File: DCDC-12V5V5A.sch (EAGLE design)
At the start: 30 parts, among them CN2 2828XX-2282834-2, CN3 2828XX-2282834-2, Q10 NMOSFET, Q9 NMOSFET, U1 LM3150MHX/NOPB

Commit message: Added board design. Added descriptive texts. Generated CAM files.
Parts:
- added LOGO1: RSNURL_QR_8MM, _my_logos:RSNURL_QR_8MM
- added LOGO2: MFDECLOGO_L_10MM, _my_logos:MFDECLOGO_L_10MM
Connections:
- net 5V: now also CN3.2; no longer CN3.1
- net GND: now also CN3.1; no longer CN3.2
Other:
- moved on the sheet: CN3
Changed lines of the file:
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@@
 <part name="GND3" library="SparkFun-PowerSymbols" library_urn="urn:adsk.eagle:library:530" deviceset="GND" device=""/>
 <part name="SUPPLY6" library="SparkFun-PowerSymbols" library_urn="urn:adsk.eagle:library:530" deviceset="5V" device=""/>
+<part name="LOGO1" library="_my_logos" deviceset="RSNURL" device="_QR_8MM" value="RSNURL_QR_8MM"/>
+<part name="LOGO2" library="_my_logos" deviceset="MFDECLOGO" device="_L_10MM" value="MFDECLOGO_L_10MM"/>
 </parts>
 <sheets>
@@
 <attribute name="VALUE" x="22.86" y="102.68" size="1.778" layer="95" rot="R180" align="center"/>
 </instance>
-<instance part="CN3" gate="G$1" x="241.3" y="106.68" smashed="yes">
-<attribute name="NAME" x="241.3" y="102.68" size="1.778" layer="95" align="center"/>
-<attribute name="VALUE" x="241.3" y="113.22" size="1.778" layer="95" align="center"/>
+<instance part="CN3" gate="G$1" x="241.3" y="109.22" smashed="yes" rot="MR180">
+<attribute name="NAME" x="241.3" y="113.22" size="1.778" layer="95" rot="MR180" align="center"/>
+<attribute name="VALUE" x="241.3" y="102.68" size="1.778" layer="95" rot="MR180" align="center"/>
 </instance>
 <instance part="GND1" gate="1" x="30.48" y="104.14" smashed="yes">
@@
 <attribute name="VALUE" x="233.68" y="112.014" size="1.778" layer="96" align="bottom-center"/>
 </instance>
+<instance part="LOGO1" gate="G$1" x="139.7" y="2.54" smashed="yes"/>
+<instance part="LOGO2" gate="G$1" x="109.22" y="2.54" smashed="yes"/>
 </instances>
 <busses>
@@
 </segment>
 <segment>
-<pinref part="CN3" gate="G$1" pin="2"/>
-<pinref part="GND3" gate="1" pin="GND"/>
-<wire x1="236.15" y1="106.68" x2="233.68" y2="106.68" width="0.1524" layer="91"/>
-</segment>
-<segment>
 <pinref part="GND1" gate="1" pin="GND"/>
 <pinref part="CN2" gate="G$1" pin="1"/>
@@
 <wire x1="30.48" y1="132.08" x2="30.48" y2="129.54" width="0.1524" layer="91"/>
 <junction x="30.48" y="129.54"/>
+</segment>
+<segment>
+<pinref part="CN3" gate="G$1" pin="1"/>
+<pinref part="GND3" gate="1" pin="GND"/>
+<wire x1="236.15" y1="106.68" x2="233.68" y2="106.68" width="0.1524" layer="91"/>
 </segment>
 </net>
@@
 </segment>
 <segment>
-<pinref part="CN3" gate="G$1" pin="1"/>
 <pinref part="SUPPLY6" gate="G$1" pin="5V"/>
-<wire x1="236.15" y1="109.22" x2="233.68" y2="109.22" width="0.1524" layer="91"/>
+<pinref part="CN3" gate="G$1" pin="2"/>
+<wire x1="233.68" y1="109.22" x2="236.15" y2="109.22" width="0.1524" layer="91"/>
 </segment>
 </net>

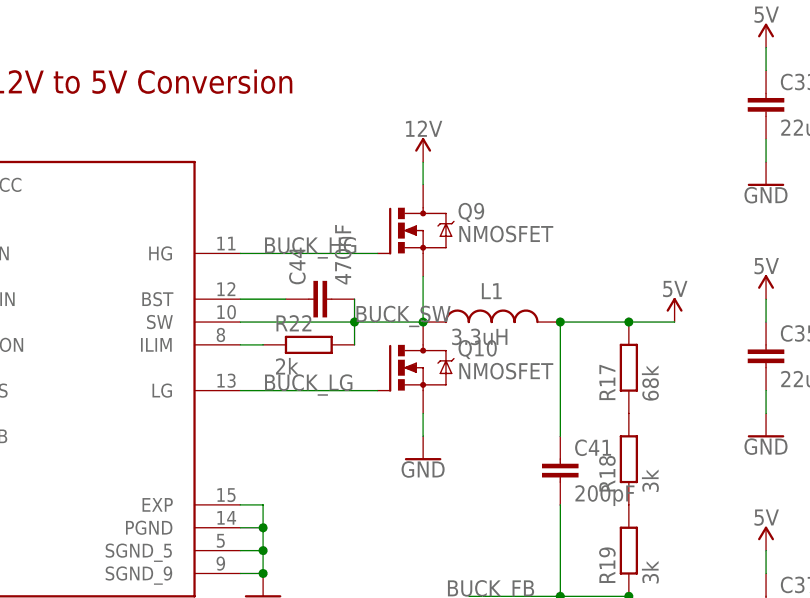
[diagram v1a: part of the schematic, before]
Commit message: Exchanged MOSFETs for bigger once. Generated CAM files. Generated BoM and PnP files.
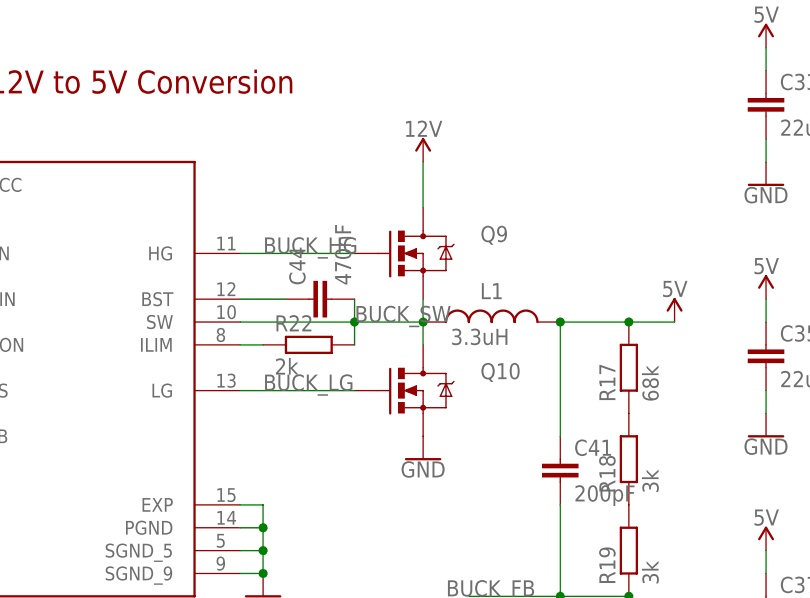
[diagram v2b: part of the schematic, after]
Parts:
- Q10, Q9: device Transistor:NMOSFET_SOT23 -> BeagleBone_Blue_R3:MOSFET-NCHANNELFDD8780
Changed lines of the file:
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@@
 <layer number="115" name="ReferenceISLANDS" color="7" fill="1" visible="no" active="yes"/>
 <layer number="116" name="Patch_BOT" color="9" fill="4" visible="yes" active="yes"/>
+<layer number="117" name="BACKMAAT1" color="7" fill="1" visible="yes" active="yes"/>
 <layer number="118" name="Rect_Pads" color="7" fill="1" visible="no" active="yes"/>
+<layer number="119" name="KAP_TEKEN" color="7" fill="1" visible="yes" active="yes"/>
+<layer number="120" name="KAP_MAAT1" color="7" fill="1" visible="yes" active="yes"/>
 <layer number="121" name="_tsilk" color="7" fill="1" visible="yes" active="yes"/>
 <layer number="122" name="_bsilk" color="7" fill="1" visible="yes" active="yes"/>
@@
 <layer number="128" name="_bValues" color="7" fill="1" visible="yes" active="yes"/>
 <layer number="129" name="Mask" color="7" fill="1" visible="yes" active="yes"/>
+<layer number="130" name="SMDSTROOK" color="7" fill="1" visible="yes" active="yes"/>
 <layer number="131" name="tAdjust" color="7" fill="1" visible="yes" active="yes"/>
 <layer number="132" name="bAdjust" color="7" fill="1" visible="yes" active="yes"/>
+<layer number="133" name="bottom_silk" color="7" fill="1" visible="yes" active="yes"/>
+<layer number="134" name="silk_top" color="7" fill="1" visible="yes" active="yes"/>
+<layer number="135" name="silk_bottom" color="7" fill="1" visible="yes" active="yes"/>
+<layer number="136" name="silktop" color="7" fill="1" visible="yes" active="yes"/>
+<layer number="137" name="silkbottom" color="7" fill="1" visible="yes" active="yes"/>
 <layer number="144" name="Drill_legend" color="7" fill="1" visible="yes" active="yes"/>
+<layer number="145" name="DrillLegend_01-16" color="7" fill="1" visible="yes" active="yes"/>
+<layer number="146" name="DrillLegend_01-20" color="7" fill="1" visible="yes" active="yes"/>
 <layer number="150" name="Notes" color="7" fill="1" visible="yes" active="yes"/>
 <layer number="151" name="HeatSink" color="7" fill="1" visible="yes" active="yes"/>
@@
 <part name="SUPPLY43" library="SparkFun-PowerSymbols" library_urn="urn:adsk.eagle:library:530" deviceset="5V" device=""/>
 <part name="U1" library="LM3150MHX_NOPB" deviceset="LM3150MHX/NOPB" device=""/>
-<part name="Q9" library="Transistor" library_urn="urn:adsk.eagle:library:16378713" deviceset="NMOSFET" device="SOT23" package3d_urn="urn:adsk.eagle:package:28738/2" technology="_" value="NMOSFET"/>
-<part name="Q10" library="Transistor" library_urn="urn:adsk.eagle:library:16378713" deviceset="NMOSFET" device="SOT23" package3d_urn="urn:adsk.eagle:package:28738/2" technology="_" value="NMOSFET"/>
+<part name="Q9" library="BeagleBone_Blue_R3" library_urn="urn:adsk.eagle:library:5828899" deviceset="MOSFET-NCHANNEL" device="FDD8780" package3d_urn="urn:adsk.eagle:package:5829549/1" value="NMOSFET"/>
+<part name="Q10" library="BeagleBone_Blue_R3" library_urn="urn:adsk.eagle:library:5828899" deviceset="MOSFET-NCHANNEL" device="FDD8780" package3d_urn="urn:adsk.eagle:package:5829549/1" value="NMOSFET"/>
 <part name="SUPPLY44" library="SparkFun-PowerSymbols" library_urn="urn:adsk.eagle:library:530" deviceset="12V" device=""/>
 <part name="GND51" library="SparkFun-PowerSymbols" library_urn="urn:adsk.eagle:library:530" deviceset="GND" device=""/>
@@
 <attribute name="VALUE" x="104.14" y="78.74" size="1.778" layer="96" ratio="10" rot="SR0"/>
 </instance>
-<instance part="Q9" gate="G$1" x="152.4" y="121.92" smashed="yes">
-<attribute name="NAME" x="158.75" y="123.19" size="1.778" layer="95"/>
-<attribute name="VALUE" x="158.75" y="120.65" size="1.778" layer="96"/>
-</instance>
-<instance part="Q10" gate="G$1" x="152.4" y="106.68" smashed="yes">
-<attribute name="NAME" x="158.75" y="107.95" size="1.778" layer="95"/>
-<attribute name="VALUE" x="158.75" y="105.41" size="1.778" layer="96"/>
+<instance part="Q9" gate="G$1" x="154.94" y="119.38" smashed="yes">
+<attribute name="NAME" x="161.29" y="120.65" size="1.778" layer="95"/>
+</instance>
+<instance part="Q10" gate="G$1" x="154.94" y="104.14" smashed="yes">
+<attribute name="NAME" x="161.29" y="105.41" size="1.778" layer="95"/>
 </instance>
 <instance part="SUPPLY44" gate="G$1" x="154.94" y="129.54" smashed="yes">
@@
 <segment>
 <pinref part="Q9" gate="G$1" pin="D"/>
-<wire x1="154.94" y1="127" x2="154.94" y2="129.54" width="0.1524" layer="91"/>
+<wire x1="154.94" y1="124.46" x2="154.94" y2="129.54" width="0.1524" layer="91"/>
 <pinref part="SUPPLY44" gate="G$1" pin="12V"/>
 </segment>
@@
 <segment>
 <pinref part="Q10" gate="G$1" pin="S"/>
-<wire x1="154.94" y1="101.6" x2="154.94" y2="99.06" width="0.1524" layer="91"/>
 <pinref part="GND51" gate="1" pin="GND"/>
 </segment>
@@
 <pinref part="U1" gate="G$1" pin="LG"/>
 <pinref part="Q10" gate="G$1" pin="G"/>
-<wire x1="134.62" y1="104.14" x2="149.86" y2="104.14" width="0.1524" layer="91"/>
+<wire x1="134.62" y1="104.14" x2="147.32" y2="104.14" width="0.1524" layer="91"/>
 <label x="137.16" y="104.14" size="1.778" layer="95"/>
 </segment>
@@
 <pinref part="U1" gate="G$1" pin="HG"/>
 <pinref part="Q9" gate="G$1" pin="G"/>
-<wire x1="134.62" y1="119.38" x2="149.86" y2="119.38" width="0.1524" layer="91"/>
+<wire x1="134.62" y1="119.38" x2="147.32" y2="119.38" width="0.1524" layer="91"/>
 <label x="137.16" y="119.38" size="1.778" layer="95"/>
 </segment>
@@
 <net name="BUCK_SW" class="0">
 <segment>
-<pinref part="Q10" gate="G$1" pin="D"/>
-<pinref part="Q9" gate="G$1" pin="S"/>
-<wire x1="154.94" y1="111.76" x2="154.94" y2="116.84" width="0.1524" layer="91"/>
 <pinref part="U1" gate="G$1" pin="SW"/>
 <wire x1="134.62" y1="111.76" x2="147.32" y2="111.76" width="0.1524" layer="91"/>
-<junction x="154.94" y="111.76"/>
-<pinref part="L1" gate="G$1" pin="1"/>
-<wire x1="147.32" y1="111.76" x2="154.94" y2="111.76" width="0.1524" layer="91"/>
 <pinref part="R22" gate="G$1" pin="2"/>
 <wire x1="147.32" y1="109.22" x2="147.32" y2="111.76" width="0.1524" layer="91"/>
@@
 <wire x1="147.32" y1="114.3" x2="147.32" y2="111.76" width="0.1524" layer="91"/>
 <label x="147.32" y="111.76" size="1.778" layer="95"/>
+<pinref part="Q10" gate="G$1" pin="D"/>
+<pinref part="L1" gate="G$1" pin="1"/>
+<wire x1="154.94" y1="109.22" x2="154.94" y2="111.76" width="0.1524" layer="91"/>
+<pinref part="Q9" gate="G$1" pin="S"/>
+<wire x1="154.94" y1="111.76" x2="154.94" y2="114.3" width="0.1524" layer="91"/>
+<junction x="154.94" y="111.76"/>
+<wire x1="154.94" y1="111.76" x2="147.32" y2="111.76" width="0.1524" layer="91"/>
 </segment>
 </net>

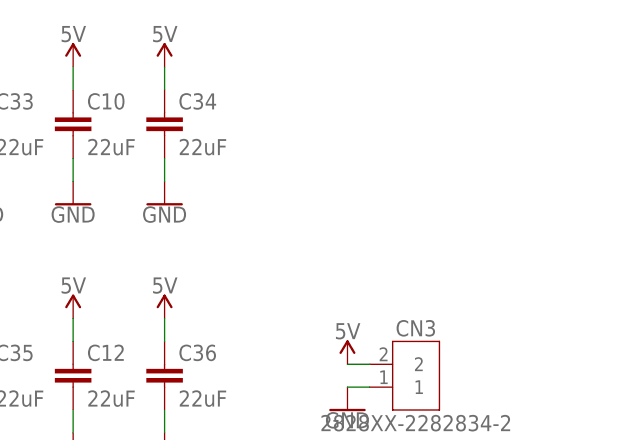
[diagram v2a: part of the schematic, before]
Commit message: Added indication LED. Generated CAM files. Generated BoM and PnP files.
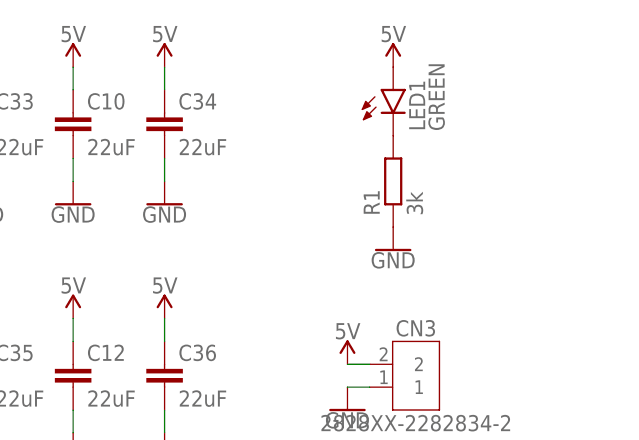
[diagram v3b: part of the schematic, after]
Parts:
- added LED1: GREEN, led:LEDSML0603
- added R1: 3k, rcl:R-EU_R0603
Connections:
- new net N$1: LED1.C, R1.2
- net 5V: now also LED1.A
- net GND: now also R1.1
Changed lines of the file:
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@@
 <part name="LOGO1" library="_my_logos" deviceset="RSNURL" device="_QR_8MM" value="RSNURL_QR_8MM"/>
 <part name="LOGO2" library="_my_logos" deviceset="MFDECLOGO" device="_L_10MM" value="MFDECLOGO_L_10MM"/>
+<part name="LED1" library="led" library_urn="urn:adsk.eagle:library:259" deviceset="LED" device="SML0603" package3d_urn="urn:adsk.eagle:package:15832/1" value="GREEN"/>
+<part name="R1" library="rcl" library_urn="urn:adsk.eagle:library:334" deviceset="R-EU_" device="R0603" package3d_urn="urn:adsk.eagle:package:23555/3" value="3k"/>
+<part name="SUPPLY7" library="SparkFun-PowerSymbols" library_urn="urn:adsk.eagle:library:530" deviceset="5V" device=""/>
+<part name="GND4" library="SparkFun-PowerSymbols" library_urn="urn:adsk.eagle:library:530" deviceset="GND" device=""/>
 </parts>
 <sheets>
@@
 <instance part="LOGO1" gate="G$1" x="139.7" y="2.54" smashed="yes"/>
 <instance part="LOGO2" gate="G$1" x="109.22" y="2.54" smashed="yes"/>
+<instance part="LED1" gate="G$1" x="238.76" y="139.7" smashed="yes">
+<attribute name="NAME" x="242.316" y="135.128" size="1.778" layer="95" rot="R90"/>
+<attribute name="VALUE" x="244.475" y="135.128" size="1.778" layer="96" rot="R90"/>
+</instance>
+<instance part="R1" gate="G$1" x="238.76" y="129.54" smashed="yes" rot="R90">
+<attribute name="NAME" x="237.2614" y="125.73" size="1.778" layer="95" rot="R90"/>
+<attribute name="VALUE" x="242.062" y="125.73" size="1.778" layer="96" rot="R90"/>
+</instance>
+<instance part="SUPPLY7" gate="G$1" x="238.76" y="142.24" smashed="yes">
+<attribute name="VALUE" x="238.76" y="145.034" size="1.778" layer="96" align="bottom-center"/>
+</instance>
+<instance part="GND4" gate="1" x="238.76" y="121.92" smashed="yes">
+<attribute name="VALUE" x="238.76" y="121.666" size="1.778" layer="96" align="top-center"/>
+</instance>
 </instances>
 <busses>
@@
 <wire x1="236.15" y1="106.68" x2="233.68" y2="106.68" width="0.1524" layer="91"/>
 </segment>
+<segment>
+<pinref part="R1" gate="G$1" pin="1"/>
+<pinref part="GND4" gate="1" pin="GND"/>
+</segment>
 </net>
 <net name="5V" class="0">
@@
 <pinref part="CN3" gate="G$1" pin="2"/>
 <wire x1="233.68" y1="109.22" x2="236.15" y2="109.22" width="0.1524" layer="91"/>
+</segment>
+<segment>
+<pinref part="LED1" gate="G$1" pin="A"/>
+<pinref part="SUPPLY7" gate="G$1" pin="5V"/>
 </segment>
 </net>
@@
 </segment>
 </net>
+<net name="N$1" class="0">
+<segment>
+<pinref part="LED1" gate="G$1" pin="C"/>
+<pinref part="R1" gate="G$1" pin="2"/>
+</segment>
+</net>
 </nets>
 </sheet>
 </sheets>
+<errors>
+</errors>
 </schematic>
 </drawing>

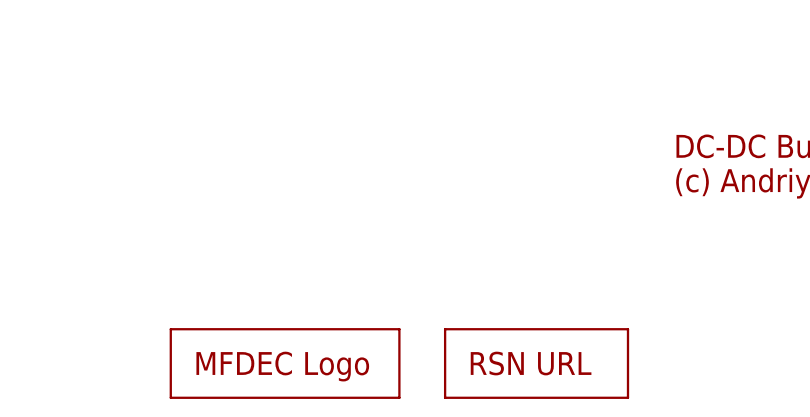
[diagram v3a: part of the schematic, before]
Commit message: Added tooling holes. Generated CAM files.
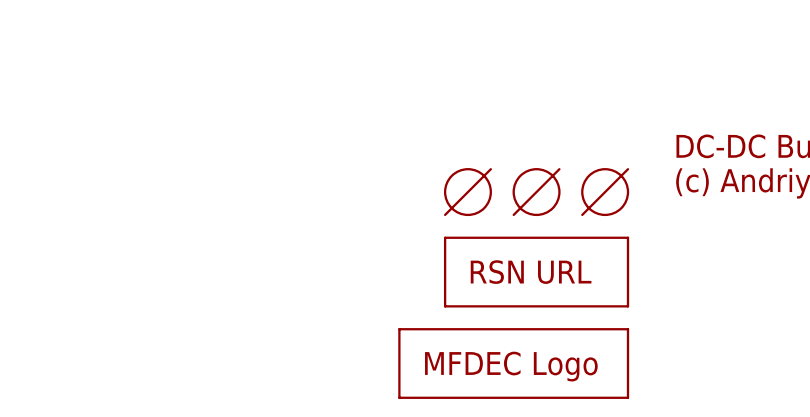
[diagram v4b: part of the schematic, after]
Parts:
- added HOLE1, HOLE2, HOLE3: TOOLINGHOLE, _my_fiducia:TOOLINGHOLE
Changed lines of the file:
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@@
 <layer number="136" name="silktop" color="7" fill="1" visible="yes" active="yes"/>
 <layer number="137" name="silkbottom" color="7" fill="1" visible="yes" active="yes"/>
+<layer number="138" name="EEE" color="7" fill="1" visible="yes" active="yes"/>
+<layer number="139" name="_tKeepout" color="7" fill="1" visible="yes" active="yes"/>
+<layer number="141" name="ASSEMBLY_TOP" color="7" fill="1" visible="yes" active="yes"/>
+<layer number="143" name="PLACE_BOUND_TOP" color="7" fill="1" visible="yes" active="yes"/>
 <layer number="144" name="Drill_legend" color="7" fill="1" visible="yes" active="yes"/>
 <layer number="145" name="DrillLegend_01-16" color="7" fill="1" visible="yes" active="yes"/>
 <layer number="146" name="DrillLegend_01-20" color="7" fill="1" visible="yes" active="yes"/>
+<layer number="147" name="PIN_NUMBER" color="7" fill="1" visible="yes" active="yes"/>
 <layer number="150" name="Notes" color="7" fill="1" visible="yes" active="yes"/>
 <layer number="151" name="HeatSink" color="7" fill="1" visible="yes" active="yes"/>
@@
 <layer number="154" name="FabDoc2" color="7" fill="1" visible="yes" active="yes"/>
 <layer number="155" name="FabDoc3" color="7" fill="1" visible="yes" active="yes"/>
+<layer number="166" name="AntennaArea" color="7" fill="1" visible="yes" active="yes"/>
+<layer number="168" name="4mmHeightArea" color="7" fill="1" visible="yes" active="yes"/>
 <layer number="199" name="Contour" color="7" fill="1" visible="yes" active="yes"/>
 <layer number="200" name="200bmp" color="1" fill="10" visible="yes" active="yes"/>
@@
 <part name="SUPPLY7" library="SparkFun-PowerSymbols" library_urn="urn:adsk.eagle:library:530" deviceset="5V" device=""/>
 <part name="GND4" library="SparkFun-PowerSymbols" library_urn="urn:adsk.eagle:library:530" deviceset="GND" device=""/>
+<part name="HOLE1" library="_my_fiducia" deviceset="TOOLINGHOLE" device=""/>
+<part name="HOLE2" library="_my_fiducia" deviceset="TOOLINGHOLE" device=""/>
+<part name="HOLE3" library="_my_fiducia" deviceset="TOOLINGHOLE" device=""/>
 </parts>
 <sheets>
@@
 <attribute name="VALUE" x="233.68" y="112.014" size="1.778" layer="96" align="bottom-center"/>
 </instance>
-<instance part="LOGO1" gate="G$1" x="139.7" y="2.54" smashed="yes"/>
-<instance part="LOGO2" gate="G$1" x="109.22" y="2.54" smashed="yes"/>
+<instance part="LOGO1" gate="G$1" x="139.7" y="12.7" smashed="yes"/>
+<instance part="LOGO2" gate="G$1" x="134.62" y="2.54" smashed="yes"/>
 <instance part="LED1" gate="G$1" x="238.76" y="139.7" smashed="yes">
 <attribute name="NAME" x="242.316" y="135.128" size="1.778" layer="95" rot="R90"/>
@@
 <attribute name="VALUE" x="238.76" y="121.666" size="1.778" layer="96" align="top-center"/>
 </instance>
+<instance part="HOLE1" gate="G$1" x="157.48" y="25.4" smashed="yes"/>
+<instance part="HOLE2" gate="G$1" x="149.86" y="25.4" smashed="yes"/>
+<instance part="HOLE3" gate="G$1" x="142.24" y="25.4" smashed="yes"/>
 </instances>
 <busses>
